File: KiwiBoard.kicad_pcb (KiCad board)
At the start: 2 copper layers, 90 x 80 mm, 27 parts, among them J1 12V Power, J2 Heater, J3 Fan, J4A1 Motor A, J4B1 Motor B, J5 OLED, J6 Encoder Connector, J7 Expansion, K1 G5LE-14 DC3, Q1 PN2222A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

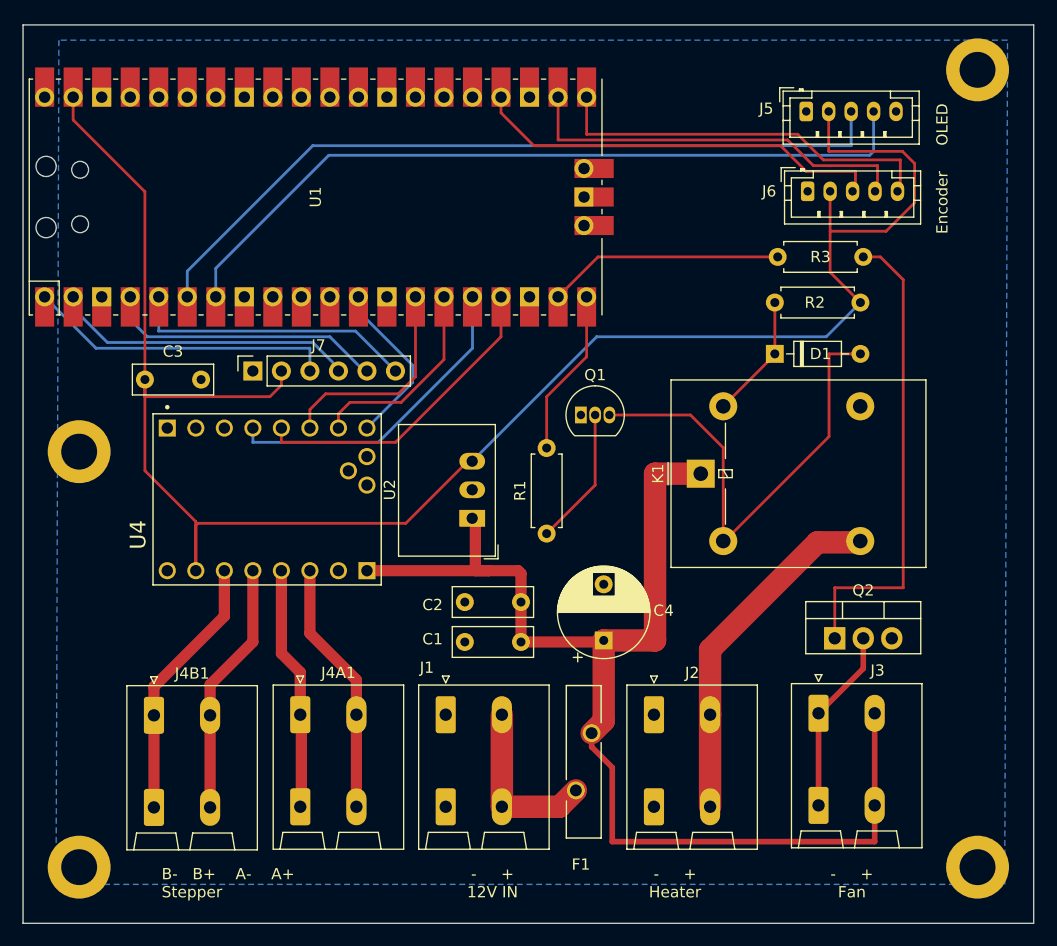
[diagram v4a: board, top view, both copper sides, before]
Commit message: Rev2 board, LCD connector, adjusted Q1 footprint.  Pico slid to edge
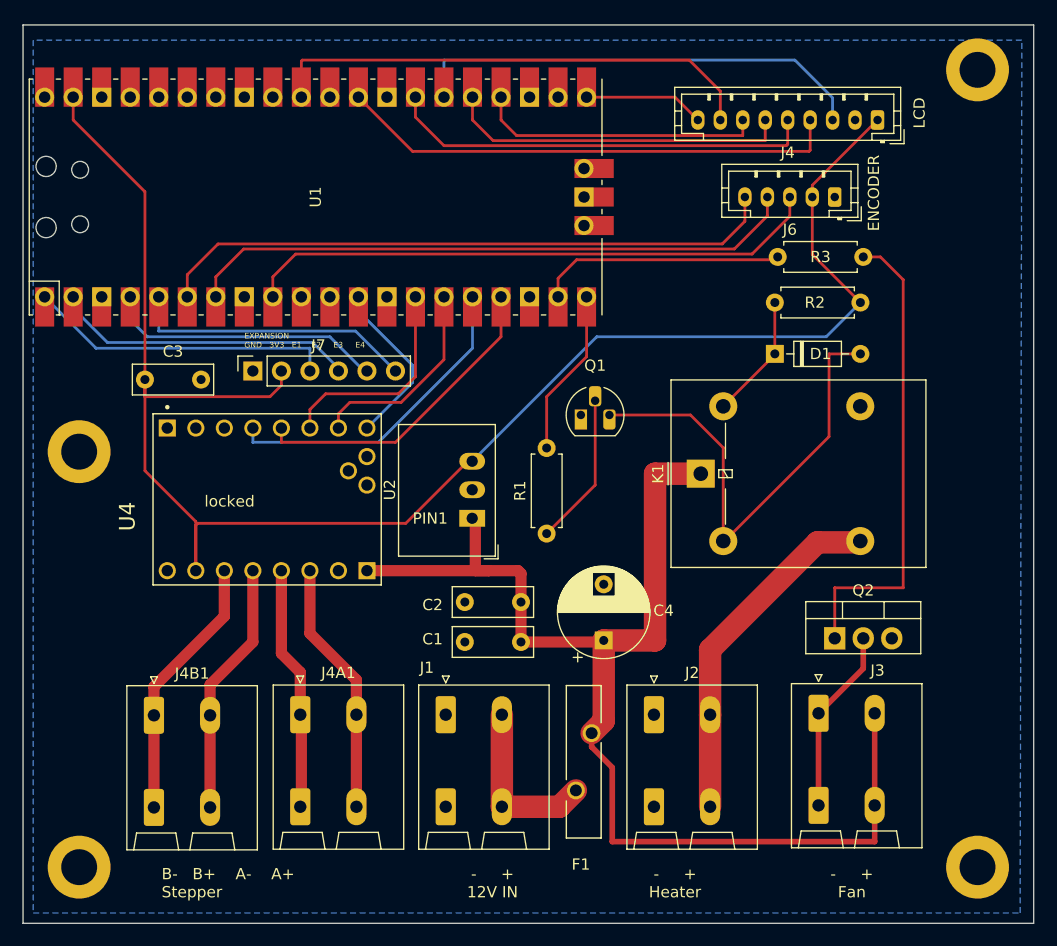
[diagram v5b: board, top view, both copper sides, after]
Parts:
- removed J5: OLED, Connector_JST:JST_PH_B5B-PH-K_1x05_P2.00mm_Vertical
- added J4: LCD, Connector_JST:JST_PH_B9B-PH-K_1x09_P2.00mm_Vertical, F.Cu at (117.1, 45.5)
- Q1: footprint Package_TO_SOT_THT:TO-92_Inline -> Package_TO_SOT_THT:TO-92_HandSolder
- moved J6 2.46 mm to (113.3, 52.3), turned to 180 degrees
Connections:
- U1 pad 21: ENC2 -> LCD_MISO
- U1 pad 22: ENC1 -> unconnected-(U1-GPIO17-Pad22)
- U1 pad 24: BTN -> LCD_SCK
- U1 pad 25: unconnected-(U1-GPIO19-Pad25) -> LCD_MOSI
- U1 pad 26: unconnected-(U1-GPIO20-Pad26) -> LCD_CS
- U1 pad 27: unconnected-(U1-GPIO21-Pad27) -> LCD_DC
- U1 pad 29: unconnected-(U1-GPIO22-Pad29) -> LCD_RESET
- U1 pad 31: unconnected-(U1-GPIO26_ADC0-Pad31) -> LCD_BKLGHT
- U1 pad 6: SDA -> ENC2
- U1 pad 7: SLC -> ENC1
- U1 pad 9: unconnected-(U1-GPIO6-Pad9) -> BTN
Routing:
- net SDA: track 69.1 -> 0.00 mm
- net SLC: track 69.0 -> 0.00 mm
- net LCD_RESET: track 0.00 -> 45.0 mm
- net LCD_BKLGHT: track 0.00 -> 44.3 mm
- net LCD_CS: track 0.00 -> 41.3 mm
- net LCD_DC: track 0.00 -> 38.2 mm
- net LCD_MOSI: track 0.00 -> 30.7 mm
- net LCD_SCK: track 0.00 -> 25.5 mm
- net ENC2: track 35.2 -> 55.8 mm
- net ENC1: track 36.3 -> 54.8 mm
- net BTN: track 37.1 -> 51.8 mm
- net +3.3V: track 167.8 -> 153.6 mm
- net LCD_MISO: track 0.00 -> 10.7 mm
- net Net-(Q1-B): track 12.4 -> 13.6 mm
- net FAN_CTL: track 21.0 -> 22.0 mm
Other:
- board text added: "ENCODER"
- board text added: "EXPANSION GND 3V3 E1 E2 E3 E4"
- board text added: "KiwiBoard Revision: 2 2023 NybbleByte"
- board text added: "LCD"
- board text added: "PIN1"
- board text added: "locked"
- board text removed: "Encoder"
- board text removed: "KiwiBoard 2023 NybbleByte"
- board text removed: "OLED"
- board text removed: "^^ INSERT ELECTRONS HERE ^^"

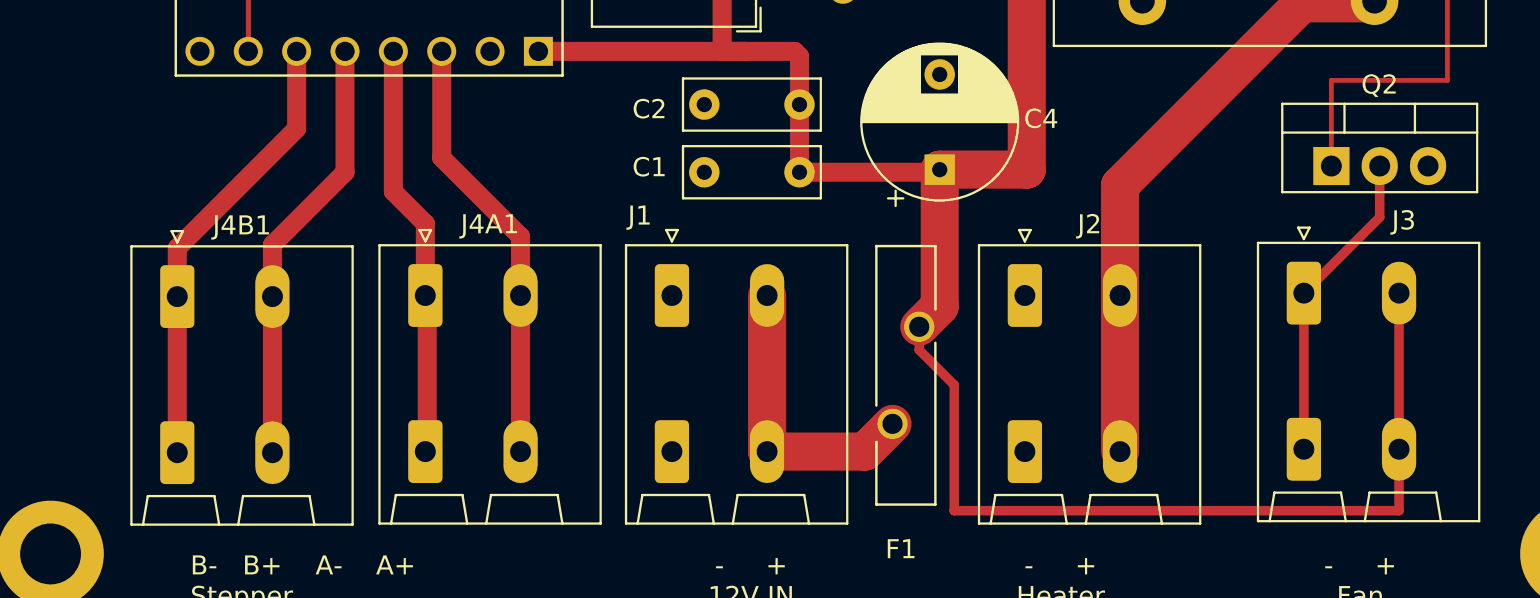
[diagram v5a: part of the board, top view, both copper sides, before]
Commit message: resize upper row of holes, add a bird
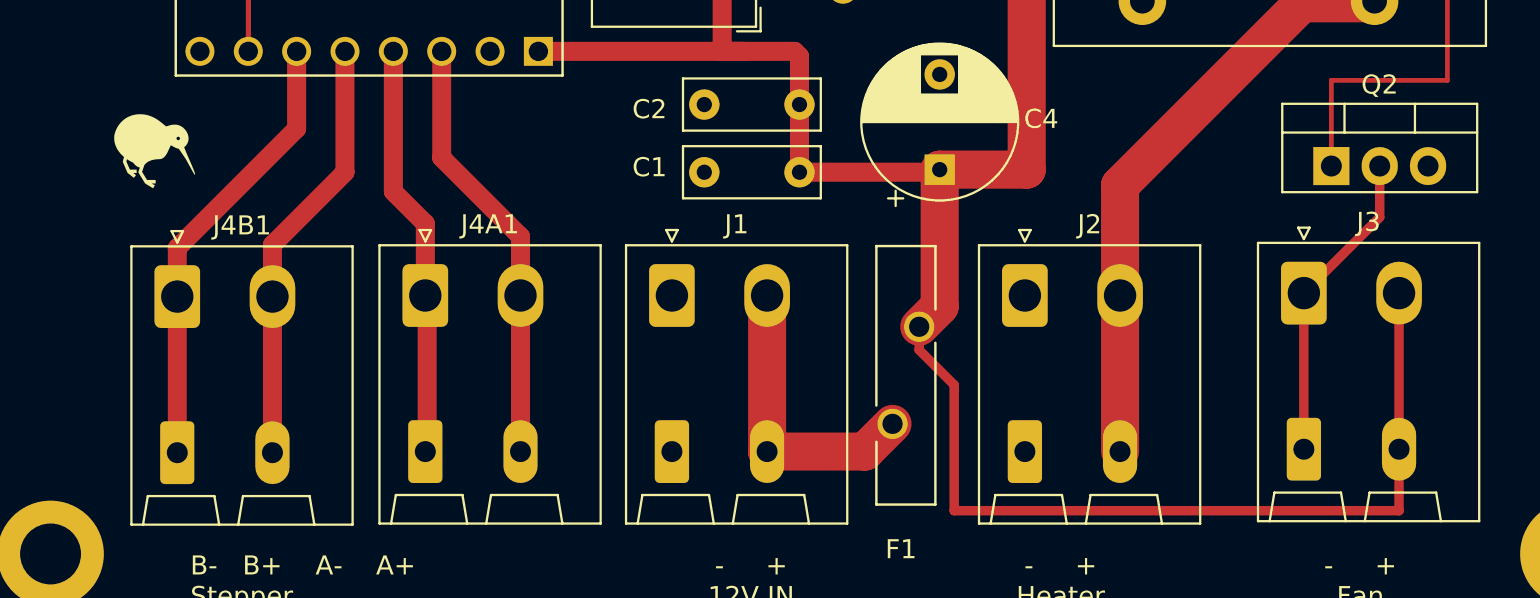
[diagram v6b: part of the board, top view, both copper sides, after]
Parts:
- J1, J2, J3, J4A1, J4B1: footprint Connector_Phoenix_SPT:PhoenixContact_SPT_2.5_2-H-5.0-EX_1x02_P5.0mm_Horizontal -> Connector_Phoenix_SPT:Kiwiboard - PhoenixContact_SPT_2.5_2-H-5.0-EX_1x02_P5.0mm_Horizontal
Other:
- board text added: "KiwiBoard Revision: 3 2023 NybbleByte"
- board text removed: "KiwiBoard Revision: 2 2023 NybbleByte"
